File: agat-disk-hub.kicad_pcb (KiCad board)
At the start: 2 copper layers, 53.3 x 61 mm, 17 parts, among them J1 IDC‐20, J2 IDC‐20, J3 IDC‐34, J4 IDC‐10, J5 KK‐4

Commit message: delete pad 5 of floppy connector J3 - pin must be removed to accomodate floppy cable with stub
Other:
- board text removed: "x"
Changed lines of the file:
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@@
 		(sheetname "/")
 		(sheetfile "agat-disk-hub.kicad_sch")
-		(units
-			(unit
-				(name "A")
-				(pins "1" "3" "5" "7" "9" "11" "13" "15" "17" "19" "21" "23" "25" "27"
-					"29" "31" "33" "2" "4" "6" "8" "10" "12" "14" "16" "18" "20" "22" "24"
-					"26" "28" "30" "32" "34"
-				)
-			)
-		)
 		(attr through_hole)
 		(duplicate_pad_numbers_are_jumpers no)
@@
 			(pintype "passive+no_connect")
 		)
-		(pad "5" thru_hole circle
-			(at 5.08 0 90)
-			(size 1.7 1.7)
-			(drill 1)
-			(layers "*.Cu" "*.Mask")
-			(remove_unused_layers no)
-			(net "unconnected-(J3-Pin_5-Pad5)")
-			(pinfunction "Pin_5_5")
-			(pintype "passive+no_connect")
-		)
 		(pad "6" thru_hole circle
 			(at 5.08 -2.54 90)
@@
 		(layer "B.SilkS")
 		(effects
-			(font
-				(size 1.27 1.27)
-				(thickness 0.15)
-				(bold yes)
-			)
-			(justify bottom mirror)
-		)
-	)
-	(gr_text "x"
-		(at 58.34 117.07 0)
-		(layer "B.SilkS")
-		(effects

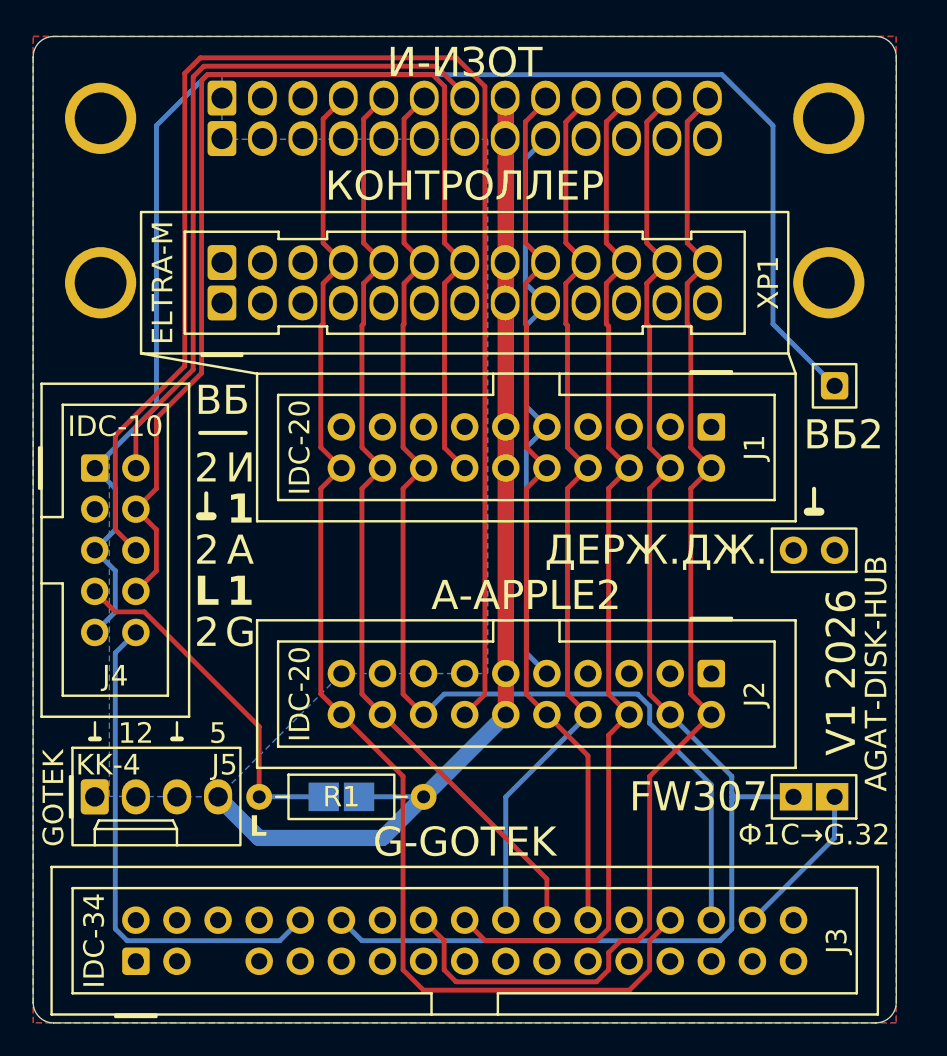
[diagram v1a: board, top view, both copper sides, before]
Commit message: remap J3 phase pins, drop FW307 jumper, restore XT1; rework symbols, silkscreen and mask
Electrical:
- J3: PH0 moves from pin 16 to pin 4, PH1 from pin 12 to pin 16, and pin 12 is left
  unconnected; tracks rerouted to match. This is needed to enable identical wiring inside Goteks
  for use with PC/Spectrum or Apple2/Agat.
- JP2, the FW307 jumper, is removed: J3 pin 32 is tied to PH1 for good - the PH0/PH1 remapping
  allows it for all use cases.
- Fixed: XT1 connector was of type 2.0 mm, now is the proper 2.54 mm (since it's just one pin, it
  defines its size); adjusted the connector position.

Schematic and symbols (refactoring only):
- XT1 is back on the schematic on DE2, after being lost together with the old JP1.
- XS404, the SNP34 cable connector, uses new project symbol SNP34-30R, whose pin names match its
  wiring.
- Eltra-26F and Eltra-26M: origin moved to pin A7, made other symbol improvements.
- J3: pin 5 is removed from the symbol copy in the schematic and from the IDC-34 library
  footprint.
- Used PWR_FLAG on GND in place of one GND symbol; made ERC exclusions for the custom footprints,
  keyed J3, and one four-way junction.
- Added note to R2 as an SMD alternative to R1, or a bridge for LEDs taking +5.
- Title block: dated 2026-10-08, deleted obsolete comment on -12|DE2.

Silkscreen and mask:
- The three museum logo footprints are replaced by the museum's name as text on F.Mask, in
  the `Agat-7 7x8px` font.
- Back: the J1 and J2 signal label rows swap places, GND texts become drawn ground marks, +5 labels
  get leader lines, pin-count labels are rotated, and row letters moved.
- Front: XS1 gets A/B row letters, the KK power connector marked as VYKHOD (output), XT1 gets a
  `(B7)` note to show its pin on the controller side.
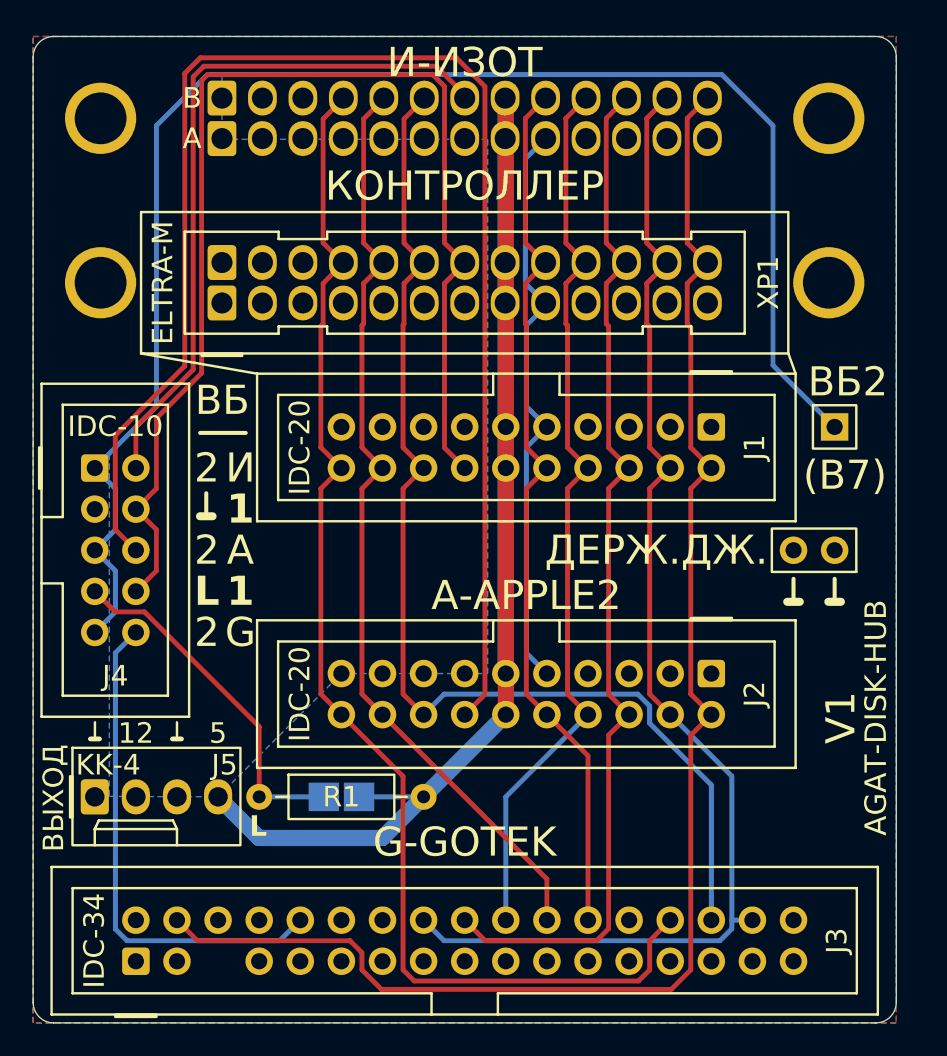
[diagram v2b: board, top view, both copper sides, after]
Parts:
- removed the G*** at (51.9, 58.9)
- removed the G*** at (51.7, 66.0)
- removed the G*** at (95.2, 58.9)
- removed JP2: PLS‐2, agat-disk-hub:jumper_pins_solder_drop_vertical
- XT1: footprint Connector_PinHeader_2.00mm:PinHeader_1x01_P2.00mm_Vertical -> Connector_PinHeader_2.54mm:PinHeader_1x01_P2.54mm_Vertical
- moved XT1 2.54 mm to (96.4, 81.5)
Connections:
- J3 pad 12: /PH1 -> unconnected-(J3-Pin_12-Pad12)
- J3 pad 16: /PH0 -> /PH1
- J3 pad 32: /J3.32 -> /PH1
- J3 pad 4: unconnected-(J3-Pin_4-Pad4) -> /PH0
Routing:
- net /PH0: track 74.5 -> 92.3 mm
- net /J3.32: track 9.72 -> 0.00 mm
- net /PH1: track 84.7 -> 77.3 mm
- net /DE2: track 93.4 -> 95.9 mm
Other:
- board text added: "(B7)"
- board text added: "34"
- board text added: "V1"
- board text added: "ВЫХОД"
- board text added: "КИБЕР"
- board text added: "МУЗЕЙ"
- board text added: "МУРОМ"
- board text removed: "32"
- board text removed: "GOTEK"
- board text removed: "J3.32"
- board text removed: "V1 2026"
- board text removed: "Ф1C→G.32"
